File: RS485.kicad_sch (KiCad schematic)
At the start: 4 parts, among them U6 SIT3485ESA

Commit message: 更新原理图
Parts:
- added C29, C30: 0.1uF, symbol Device:C
- added R8: 10K, symbol Device:R_US
- added U7: CA-IS3731HN, kicad_api_lib:CA-IS3731HN, symbol CA-IS3731HN:CA-IS3731HW
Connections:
- net CTRL: now also U7.12 (B3)
- net UART_RXD: now also U7.13 (B2)
- net UART_TXD: now also U7.14 (B1)
- net VCC: now also C29.2, C30.2, U7.1 (VDDA), U7.10 (ENB), U7.16 (VDDB), U7.7 (ENA)
- new net: R8.2, U7.5 (A3)
- new net Earth: C29.1, C30.1, U7.15 (GNDB), U7.2 (GNDA), U7.8 (GNDA), U7.9 (GNDB)
- new net RS485_DE: R8.1
- new net RS485_RX: U7.4 (A2)
- new net RS485_TX: U7.3 (A1)
- no-connect marks 0 -> 2
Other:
- moved on the sheet: C36, R18, R19, U6

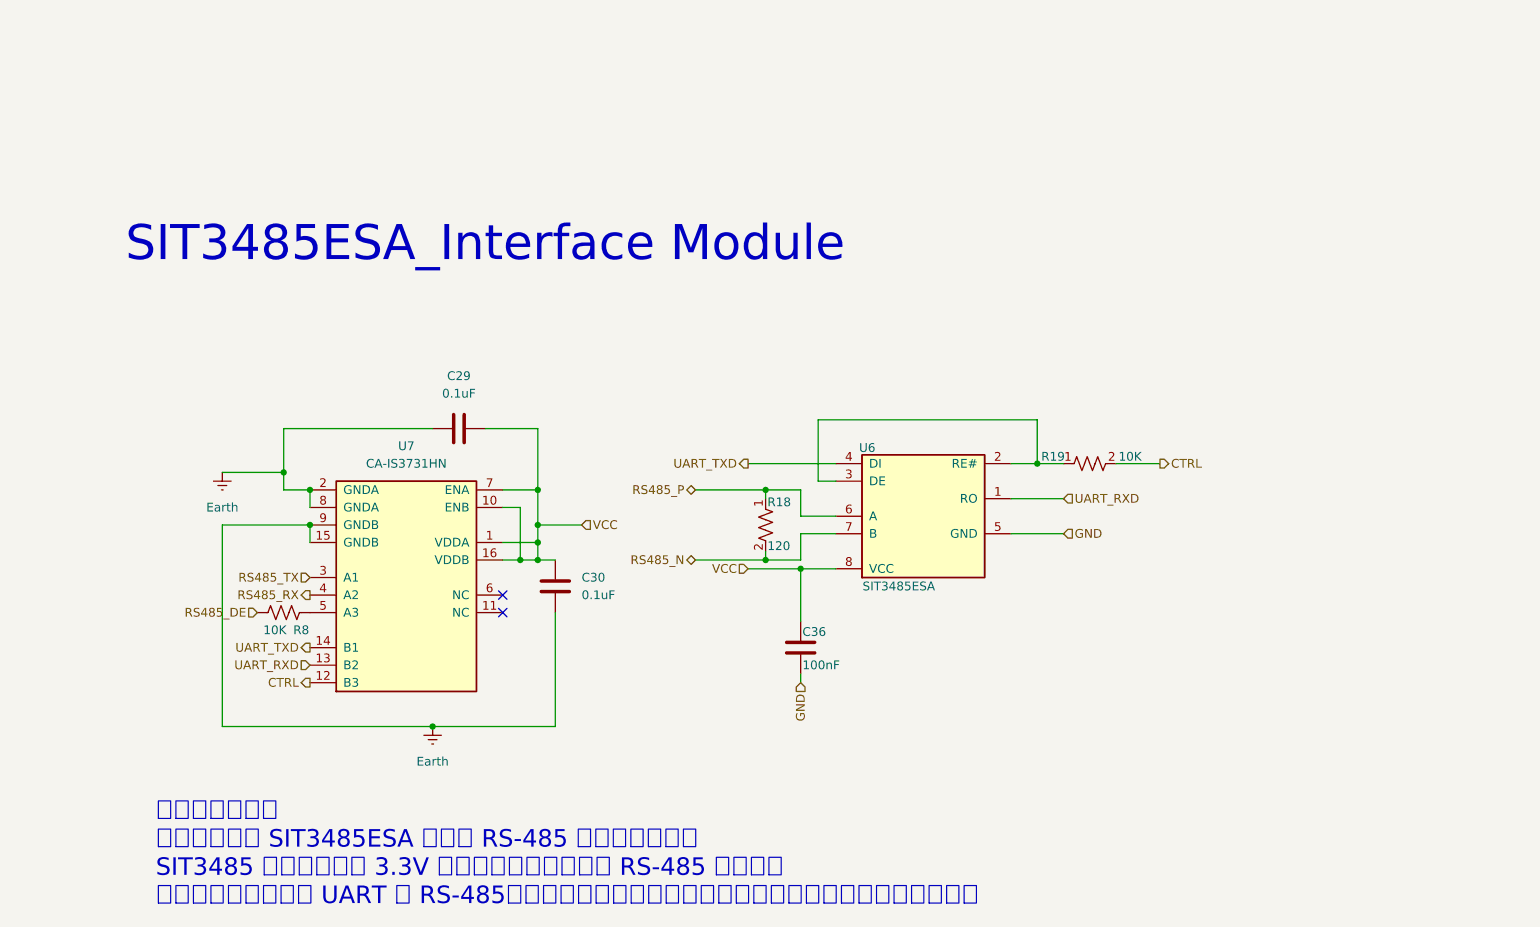
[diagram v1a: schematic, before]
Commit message: 增加USB,TYPEC转串口esd隔离，
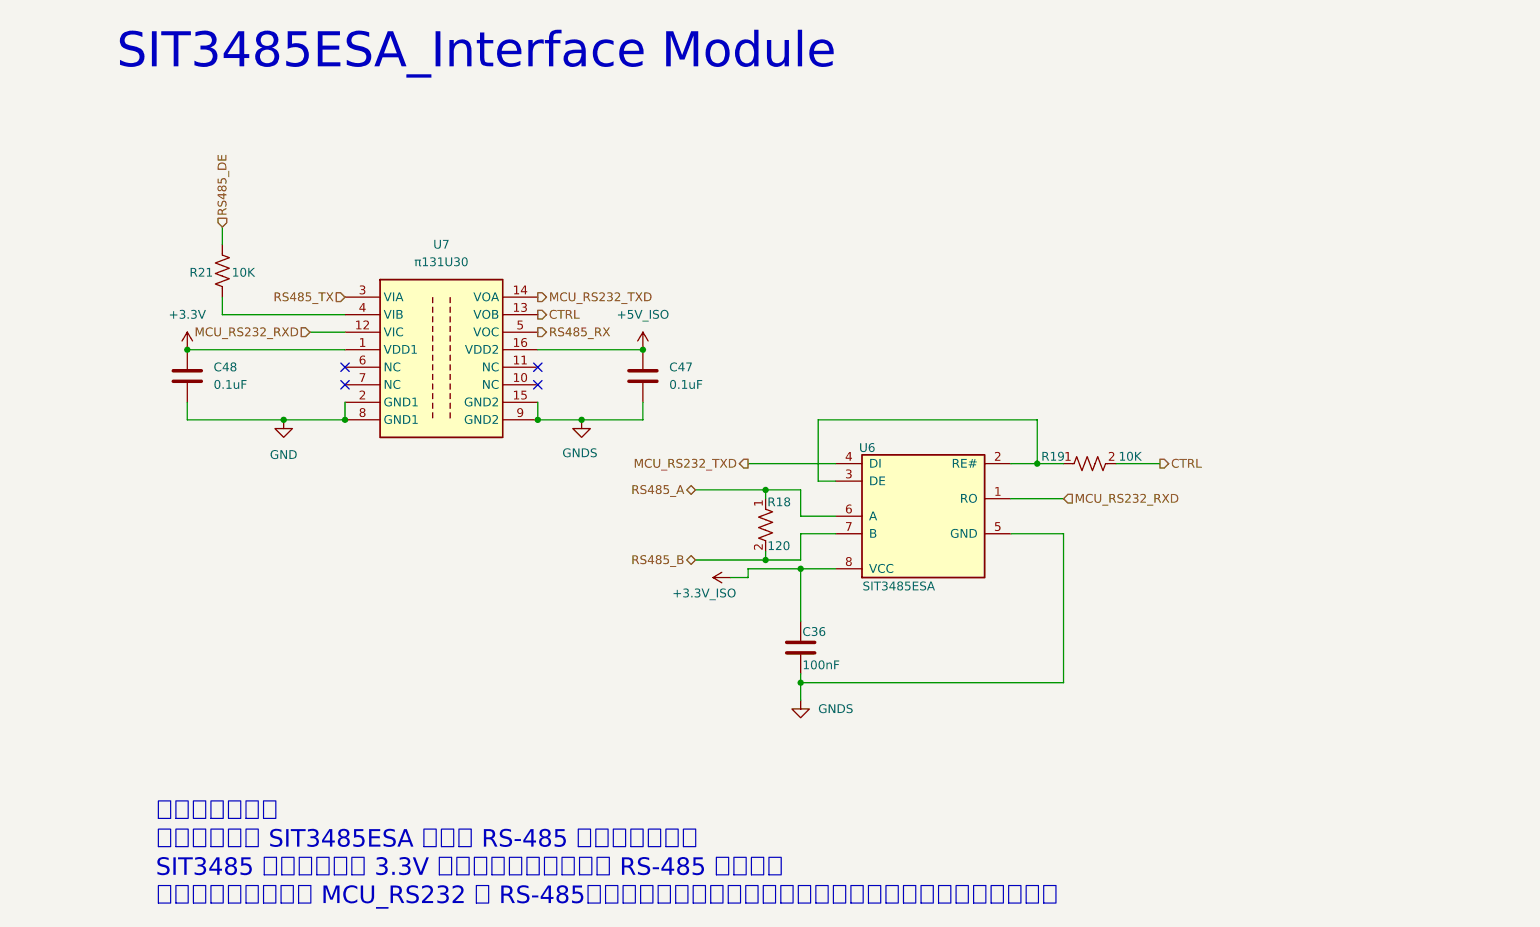
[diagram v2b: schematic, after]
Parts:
- removed C29, C30: 0.1uF, symbol Device:C
- removed R8: 10K, symbol Device:R_US
- removed U7: CA-IS3731HN, kicad_api_lib:CA-IS3731HN, symbol CA-IS3731HN:CA-IS3731HW
- added C47, C48: 0.1uF, symbol Device:C
- added R21: 10K, symbol Device:R_US
- added U7: π131U30, kicad_api_lib:π131U30, symbol π131U30:PAI_π131X3X
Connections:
- net CTRL: now also U7.13 (VOB)
- net GND: now also C48.1, U7.2 (GND1), U7.8 (GND1); no longer C36.2, U6.5 (GND)
- net RS485_DE: now also R21.2
- net RS485_RX: now also U7.5 (VOC)
- net RS485_TX: now also U7.3 (VIA)
- net RS485_N renamed RS485_B
- net RS485_P renamed RS485_A
- net UART_RXD renamed MCU_RS232_RXD
- net MCU_RS232_RXD: now also U7.12 (VIC)
- net UART_TXD renamed MCU_RS232_TXD
- net MCU_RS232_TXD: now also U7.14 (VOA)
- net VCC renamed +3.3V_ISO
- new net: R21.1, U7.4 (VIB)
- new net +3.3V: C48.2, U7.1 (VDD1)
- new net +5V_ISO: C47.2, U7.16 (VDD2)
- new net GNDS: C36.2, C47.1, U6.5 (GND), U7.15 (GND2), U7.9 (GND2)
- no-connect marks 2 -> 4
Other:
- note added: "模块电路功能： 这是一个基于 SIT3485ESA 芯片的 RS-485 通信接口电路。 SIT3485 是一款常用的 3.3V 供电、半双工、低功耗 RS-485 收发器。 该电路的功能是实现 MCU_RS232 转 RS-485。它的设计标准且完整，包含了必要的去耦电容和终端电阻。"
- note removed: "模块电路功能： 这是一个基于 SIT3485ESA 芯片的 RS-485 通信接口电路。 SIT3485 是一款常用的 3.3V 供电、半双工、低功耗 RS-485 收发器。 该电路的功能是实现 UART 转 RS-485。它的设计标准且完整，包含了必要的去耦电容和终端电阻。"

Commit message: 完成GD32F303控制板原理图与PCB设计
- 更新电源、CAN、RS232、RS485及电机通信子电路
- 切换并完善GD32F303VCT6核心原理图
- 新增PCB布局及所需符号、封装库文件
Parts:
- added CN5: WJ15EDGRC-3.81-2P, kicad_api_lib:WJ15EDGRC-3.81-2P, symbol WJ15EDGRC-3.81-2P:31330102
- C42: renamed from C48; footprint (none) -> Capacitor_SMD:C_0603_1608Metric_Pad1.08x0.95mm_HandSolder
- C43: renamed from C47; footprint (none) -> Capacitor_SMD:C_0603_1608Metric_Pad1.08x0.95mm_HandSolder
- C44: renamed from C36; footprint kicad_api_lib:0402X104K160CT -> Capacitor_SMD:C_0402_1005Metric_Pad0.74x0.62mm_HandSolder
- R16: renamed from R21; footprint (none) -> Resistor_SMD:R_0603_1608Metric_Pad0.98x0.95mm_HandSolder
- R17: renamed from R18; footprint kicad_api_lib:CRCW0603120RFKEA -> Resistor_SMD:R_0603_1608Metric_Pad0.98x0.95mm_HandSolder
- R18: renamed from R19; footprint kicad_api_lib:AF0603JR-0710KL -> Resistor_SMD:R_0603_1608Metric_Pad0.98x0.95mm_HandSolder
- U10: renamed from U6; footprint kicad_api_lib:SIT3485ESA -> Package_SO:SOIC-8_3.9x4.9mm_P1.27mm
- renumbered U7 to U9
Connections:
- net MCU_RS232_TXD is gone; now on net RS485_TX: U10.4 (DI), U9.14 (VOA)
- net RS485_A: now also CN5.2
- net RS485_B: now also CN5.1; no longer R17.2, U10.7 (B)
- net RS485_RX: now also U10.1 (RO)
- net RS485_TX: no longer U9.3 (VIA)
- net MCU_RS232_RXD renamed MCU_RS485_RXD
- net MCU_RS485_RXD: no longer U10.1 (RO)
- net RS485_DE renamed MCU_RS485_DE
- new net MCU_RS485_TX: U9.3 (VIA)
- new net RS485B: R17.2, U10.7 (B)

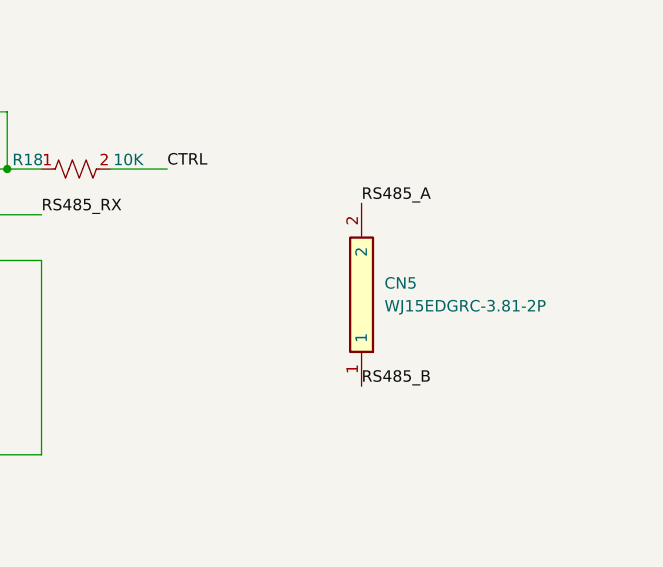
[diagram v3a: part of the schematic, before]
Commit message: 优化接口原理图与PCB布局
- 精简CAN接口并调整各子页器件编号
- 更新电源输入端子与Type-C接口封装
- 重新整理控制板PCB器件布局
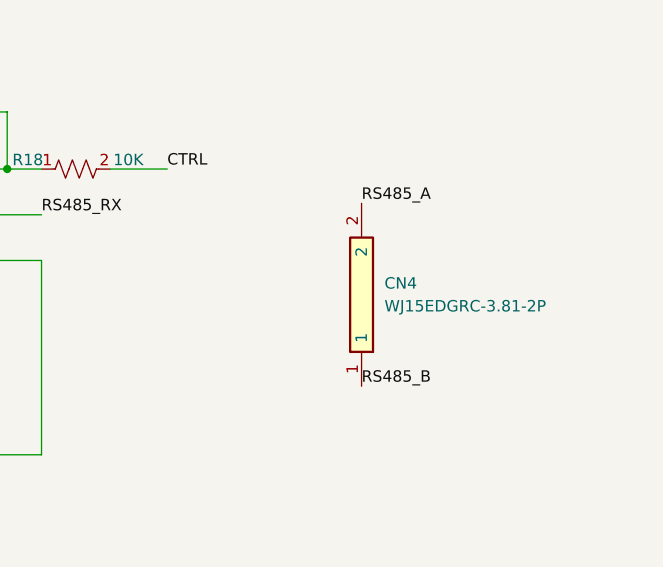
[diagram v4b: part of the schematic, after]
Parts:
- renumbered CN5 to CN4
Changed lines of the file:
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@@
 		(dnp no)
 		(fields_autoplaced yes)
-		(property "Reference" "CN5"
+		(property "Reference" "CN4"
 			(at 247.65 93.9799 90)
 			(show_name no)
@@
 			(project "GD32F303"
 				(path "/54005433-e3aa-4693-8f75-bb73943288d3/0c884452-aecc-4e2c-81cc-965ac67a1a2e"
-					(reference "CN5")
+					(reference "CN4")
 					(unit 1)
 				)

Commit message: 完善PCB布线与接口电源网络
- 调整控制板PCB器件布局与走线
- 更新MCU、电源及通信接口原理图
- 统一隔离接口地和电源网络标签并修正封装属性
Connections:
- net RS485_B is gone; now on net RS485A: CN4.1
- net RS485B: now also CN4.2
- net +3.3V_ISO renamed +3V3_ISO
- net RS485_A renamed RS485A
- net RS485A: no longer CN4.2
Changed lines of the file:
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@@
 	(wire
 		(pts
+			(xy 245.11 110.998) (xy 245.11 105.41)
+		)
+		(stroke
+			(width 0)
+			(type default)
+		)
+	)
+	(wire
+		(pts
 			(xy 176.53 91.44) (xy 171.45 91.44)
 		)
@@
 	(wire
 		(pts
+			(xy 245.11 79.248) (xy 245.11 85.09)
+		)
+		(stroke
+			(width 0)
+			(type default)
+		)
+	)
+	(wire
+		(pts
 			(xy 161.29 97.79) (xy 163.83 97.79)
 		)
@@
 		)
 	)
-	(label "RS485_A"
+	(label "RS485A"
 		(at 156.21 85.09 0)
 		(effects
@@
 		)
 	)
-	(label "RS485_RX"
-		(at 133.35 62.23 0)
+	(label "RS485A"
+		(at 245.11 110.998 0)
 		(effects
 			(font
@@
 	)
 	(label "RS485_RX"
-		(at 209.55 86.36 0)
+		(at 133.35 62.23 0)
 		(effects
 			(font
@@
 		)
 	)
-	(label "CTRL"
-		(at 133.35 59.69 0)
+	(label "RS485B"
+		(at 245.11 79.248 0)
 		(effects
 			(font
@@
 		)
 	)
-	(label "RS485_A"
-		(at 245.11 85.09 0)
+	(label "RS485_RX"
+		(at 209.55 86.36 0)
 		(effects
 			(font
@@
 		)
 	)
-	(label "RS485_B"
-		(at 245.11 105.41 0)
+	(label "CTRL"
+		(at 133.35 59.69 0)
 		(effects
 			(font
@@
 			)
 		)
-		(property "Value" "+3.3V_ISO"
+		(property "Value" "+3V3_ISO"
 			(at 157.48 100.076 90)
 			(show_name no)
@@
 	(group "SIT3485ESA_Interface Module"
 		(members "03a8f350-16e7-4e54-bb91-b1271fd25f7a" "23dfa473-4469-4f38-9314-589935e126c4"
-			"26108246-1be3-418f-a1b5-7bad52adde01" "2b41001d-9cc9-4632-a7f6-8042c0941b51"
-			"31ddb25e-b6ab-4ced-8fe1-ae8fd7e62b07" "39d72b1f-3389-4232-b2b7-e1027b86fc17"
-			"443484ec-33f8-42ee-8fbe-9dcb6f0eab62" "51d99099-4acd-4cfe-9e93-c93f0b295e31"
-			"55e09955-f414-4e01-bfcd-fa6c38337f1d" "5ed6cc2d-ccac-414a-bf56-461902222bb2"
-			"6140e6fe-5a83-46ff-9bce-0f7ebcf9845a" "62dfcb28-a389-46d6-ba56-12e3dff38496"
-			"6395606e-565f-416a-b7f2-155000fc9816" "6b1a0329-4171-4786-ab80-74d0023dd190"
-			"7c5fdb95-2271-450f-9337-2569b4fe3a41" "911a547e-cc1d-4754-95f0-e97177cc3de2"
-			"91c43ad4-cd65-4974-b441-99beb5d14579" "91f5d9a9-d8d1-4523-9239-8b167ad28e6b"
-			"9d5c04d1-a0da-457a-ba9b-5bc4c24853bf" "9e0f76fc-b6ad-415d-96c8-e3aea2d579fc"
-			"9e2a6550-1d09-4560-bf3a-ec5f651006ee" "a14a0c84-2535-4d47-9724-8012e6529ddb"
+			"26108246-1be3-418f-a1b5-7bad52adde01" "297966c9-6dc6-4762-9531-585c081aefe6"
+			"2b41001d-9cc9-4632-a7f6-8042c0941b51" "31ddb25e-b6ab-4ced-8fe1-ae8fd7e62b07"
+			"39d72b1f-3389-4232-b2b7-e1027b86fc17" "443484ec-33f8-42ee-8fbe-9dcb6f0eab62"
+			"51d99099-4acd-4cfe-9e93-c93f0b295e31" "55e09955-f414-4e01-bfcd-fa6c38337f1d"
+			"5ed6cc2d-ccac-414a-bf56-461902222bb2" "6140e6fe-5a83-46ff-9bce-0f7ebcf9845a"
+			"62dfcb28-a389-46d6-ba56-12e3dff38496" "6395606e-565f-416a-b7f2-155000fc9816"
+			"6b1a0329-4171-4786-ab80-74d0023dd190" "74e8b89f-2b7b-4e33-af30-98d2808c7b00"
+			"7c5fdb95-2271-450f-9337-2569b4fe3a41" "85949e1d-b856-4582-aba4-5c2c3af4942d"
+			"911a547e-cc1d-4754-95f0-e97177cc3de2" "91c43ad4-cd65-4974-b441-99beb5d14579"
+			"91f5d9a9-d8d1-4523-9239-8b167ad28e6b" "9d5c04d1-a0da-457a-ba9b-5bc4c24853bf"
+			"9e0f76fc-b6ad-415d-96c8-e3aea2d579fc" "9e2a6550-1d09-4560-bf3a-ec5f651006ee"
 			"a2c2a655-3083-4d99-9996-2dea564f73bf" "a9ec83d8-c6ab-43e8-be1c-8cf4f626aac8"
-			"ab71dfce-46fb-49cc-9cfb-46a799fb2d48" "b3aac39a-25d6-497d-a2c7-c40feb76406f"
-			"b5a734af-4b1c-4642-9e99-e5ce70eb4072" "b7dba2d2-eec2-4923-8ac6-fd37550d249b"
-			"b8038749-188b-4218-8d17-842c1396e420" "bc5cd577-1e5e-4f90-aaf9-22c387c5b9c7"
-			"bfbfbedd-97da-4211-ba99-46998d19c44e" "c67948f3-25a3-4b53-ab45-17b7d4af9585"
-			"cb720ff4-dc0d-412f-b55f-f07bb3dd1bd7" "cbe8c850-df89-474c-a9ca-2bf6c4b39290"
-			"cc885663-8a0d-48e5-8458-7c62c6453b33" "d0d78a06-ba3a-4898-aff4-5f6b6f7b6fa8"
-			"d2467b82-d4ce-445e-8d2a-6adb26260aa8" "d8c2b88a-e5a2-4701-a8e7-d50ea2202197"
-			"d94ab396-6e04-47c4-8b06-94bd16d04516" "daebe6e3-4e2d-444b-b451-8a02f5898537"
-			"e22e755f-e53a-4c4c-ab14-083374453ef6" "ebf69372-e787-4354-a53e-7b597cbd503f"
-			"ed190d79-050e-4e15-9d3c-59789546445f" "eea1b2e9-26ed-4bef-9e3e-f096e30246c9"
-			"ef2ebefc-983b-4848-9a18-9d586aee4b7c" "f08841d5-75c3-41d6-b8de-9fecd535c3ce"
+			"b3aac39a-25d6-497d-a2c7-c40feb76406f" "b5a734af-4b1c-4642-9e99-e5ce70eb4072"
+			"b7dba2d2-eec2-4923-8ac6-fd37550d249b" "b8038749-188b-4218-8d17-842c1396e420"
+			"bc5cd577-1e5e-4f90-aaf9-22c387c5b9c7" "bfbfbedd-97da-4211-ba99-46998d19c44e"
+			"c67948f3-25a3-4b53-ab45-17b7d4af9585" "cb720ff4-dc0d-412f-b55f-f07bb3dd1bd7"
+			"cbe8c850-df89-474c-a9ca-2bf6c4b39290" "cc885663-8a0d-48e5-8458-7c62c6453b33"
+			"d0d78a06-ba3a-4898-aff4-5f6b6f7b6fa8" "d2467b82-d4ce-445e-8d2a-6adb26260aa8"
+			"d8c2b88a-e5a2-4701-a8e7-d50ea2202197" "d94ab396-6e04-47c4-8b06-94bd16d04516"
+			"daebe6e3-4e2d-444b-b451-8a02f5898537" "e22e755f-e53a-4c4c-ab14-083374453ef6"
+			"ebf69372-e787-4354-a53e-7b597cbd503f" "ed190d79-050e-4e15-9d3c-59789546445f"
+			"eea1b2e9-26ed-4bef-9e3e-f096e30246c9" "ef2ebefc-983b-4848-9a18-9d586aee4b7c"
+			"f08841d5-75c3-41d6-b8de-9fecd535c3ce" "f54a7dd2-8bd2-499d-b4d6-678f2f426bd6"
 			"fdd4bf25-51b0-4703-9236-d98b0b2e5368" "fde634bd-a756-4e03-b0ca-3d5b3de6ddfc"
 		)

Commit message: 完善总线映射并划分隔离地与电源平面
统一3V3电源网络并消除ERC错误；优化GND/Earth耦合器件布局；完成In1.Cu地平面及In2.Cu电源平面分区。
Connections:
- net RS485A: now also CN4.2; no longer CN4.1
- net RS485B: now also CN4.1; no longer CN4.2
- net +3.3V renamed +3V3
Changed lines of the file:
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@@
 		)
 	)
-	(label "RS485A"
+	(label "RS485B"
 		(at 245.11 110.998 0)
 		(effects
@@
 		)
 	)
-	(label "RS485B"
+	(label "RS485A"
 		(at 245.11 79.248 0)
 		(effects
@@
 			)
 		)
-		(property "Value" "+3.3V"
+		(property "Value" "+3V3"
 			(at 82.55 59.69 0)
 			(show_name no)

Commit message: 更新六层控制板设计及嘉立创生产文件
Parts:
- renumbered C42 to C43, C43 to C44, C44 to C45, R16 to R18, R17 to R19, R18 to R20
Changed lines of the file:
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@@
 		(in_pos_files yes)
 		(dnp no)
-		(property "Reference" "#PWR055"
+		(property "Reference" "#PWR061"
 			(at 139.7 81.28 0)
 			(hide yes)
@@
 			(project "GD32F303VET6_4Motor_Control"
 				(path "/54005433-e3aa-4693-8f75-bb73943288d3/0c884452-aecc-4e2c-81cc-965ac67a1a2e"
-					(reference "#PWR055")
+					(reference "#PWR061")
 					(unit 1)
 				)
@@
 		(dnp no)
 		(fields_autoplaced yes)
-		(property "Reference" "C43"
+		(property "Reference" "C44"
 			(at 152.4 67.3099 0)
 			(show_name no)
@@
 			(project "GD32F303VET6_4Motor_Control"
 				(path "/54005433-e3aa-4693-8f75-bb73943288d3/0c884452-aecc-4e2c-81cc-965ac67a1a2e"
-					(reference "C43")
+					(reference "C44")
 					(unit 1)
 				)
@@
 		(dnp no)
 		(fields_autoplaced yes)
-		(property "Reference" "#PWR058"
+		(property "Reference" "#PWR064"
 			(at 171.45 121.92 0)
 			(hide yes)
@@
 			(project "GD32F303VET6_4Motor_Control"
 				(path "/54005433-e3aa-4693-8f75-bb73943288d3/0c884452-aecc-4e2c-81cc-965ac67a1a2e"
-					(reference "#PWR058")
+					(reference "#PWR064")
 					(unit 1)
 				)
@@
 		(in_pos_files yes)
 		(dnp no)
-		(property "Reference" "C44"
+		(property "Reference" "C45"
 			(at 171.704 105.664 0)
 			(show_name no)
@@
 			(project "GD32F303VET6_4Motor_Control"
 				(path "/54005433-e3aa-4693-8f75-bb73943288d3/0c884452-aecc-4e2c-81cc-965ac67a1a2e"
-					(reference "C44")
+					(reference "C45")
 					(unit 1)
 				)
@@
 		(dnp no)
 		(fields_autoplaced yes)
-		(property "Reference" "#PWR053"
+		(property "Reference" "#PWR059"
 			(at 82.55 68.58 0)
 			(hide yes)
@@
 			(project "GD32F303VET6_4Motor_Control"
 				(path "/54005433-e3aa-4693-8f75-bb73943288d3/0c884452-aecc-4e2c-81cc-965ac67a1a2e"
-					(reference "#PWR053")
+					(reference "#PWR059")
 					(unit 1)
 				)
@@
 		(in_pos_files yes)
 		(dnp no)
-		(property "Reference" "#PWR057"
+		(property "Reference" "#PWR063"
 			(at 165.1 97.79 0)
 			(hide yes)
@@
 			(project "GD32F303VET6_4Motor_Control"
 				(path "/54005433-e3aa-4693-8f75-bb73943288d3/0c884452-aecc-4e2c-81cc-965ac67a1a2e"
-					(reference "#PWR057")
+					(reference "#PWR063")
 					(unit 1)
 				)
@@
 		(in_pos_files yes)
 		(dnp no)
-		(property "Reference" "R17"
+		(property "Reference" "R19"
 			(at 166.624 86.868 0)
 			(show_name no)
@@
 			(project "GD32F303VET6_4Motor_Control"
 				(path "/54005433-e3aa-4693-8f75-bb73943288d3/0c884452-aecc-4e2c-81cc-965ac67a1a2e"
-					(reference "R17")
+					(reference "R19")
 					(unit 1)
 				)
@@
 		(dnp no)
 		(fields_autoplaced yes)
-		(property "Reference" "#PWR054"
+		(property "Reference" "#PWR060"
 			(at 96.52 81.28 0)
 			(hide yes)
@@
 			(project "GD32F303VET6_4Motor_Control"
 				(path "/54005433-e3aa-4693-8f75-bb73943288d3/0c884452-aecc-4e2c-81cc-965ac67a1a2e"
-					(reference "#PWR054")
+					(reference "#PWR060")
 					(unit 1)
 				)
@@
 		(in_pos_files yes)
 		(dnp no)
-		(property "Reference" "R16"
+		(property "Reference" "R18"
 			(at 84.582 53.594 0)
 			(show_name no)
@@
 			(project "GD32F303VET6_4Motor_Control"
 				(path "/54005433-e3aa-4693-8f75-bb73943288d3/0c884452-aecc-4e2c-81cc-965ac67a1a2e"
-					(reference "R16")
+					(reference "R18")
 					(unit 1)
 				)
@@
 		(dnp no)
 		(fields_autoplaced yes)
-		(property "Reference" "#PWR056"
+		(property "Reference" "#PWR062"
 			(at 148.59 68.58 0)
 			(hide yes)
@@
 			(project "GD32F303VET6_4Motor_Control"
 				(path "/54005433-e3aa-4693-8f75-bb73943288d3/0c884452-aecc-4e2c-81cc-965ac67a1a2e"
-					(reference "#PWR056")
+					(reference "#PWR062")
 					(unit 1)
 				)
@@
 		(in_pos_files yes)
 		(dnp no)
-		(property "Reference" "R18"
+		(property "Reference" "R20"
 			(at 208.026 80.264 90)
 			(show_name no)
@@
 			(project "GD32F303VET6_4Motor_Control"
 				(path "/54005433-e3aa-4693-8f75-bb73943288d3/0c884452-aecc-4e2c-81cc-965ac67a1a2e"
-					(reference "R18")
+					(reference "R20")
 					(unit 1)
 				)
@@
 		(dnp no)
 		(fields_autoplaced yes)
-		(property "Reference" "C42"
+		(property "Reference" "C43"
 			(at 86.36 67.3099 0)
 			(show_name no)
@@
 			(project "GD32F303VET6_4Motor_Control"
 				(path "/54005433-e3aa-4693-8f75-bb73943288d3/0c884452-aecc-4e2c-81cc-965ac67a1a2e"
-					(reference "C42")
+					(reference "C43")
 					(unit 1)
 				)
